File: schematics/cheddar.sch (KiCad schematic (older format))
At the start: 31 parts, among them J1 BATT_CONN, J2 EXTERNAL_TRIGGER, J3 USB_OTG, J4 Conn_01x08, J5 Conn_01x08, Q1 MOSFET_PCH, SW1 SW_Push, U1 ESP-12E, U2 ch340g, U3 MCP73831, U4 HT7333, Y1 12Mhz

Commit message: add symbols to schematic
remove redundant symbol libs (KiCAD version 5 has them already)
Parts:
- removed URLAB-LOGO1: logo, custom-cheddar:urlab, symbol SFE_LOGO_FLAME.1_INCH
- C1, C2, C3, C6, C7, C8, C9: symbol C_Small -> Device:C_Small
- C4, C5: symbol C -> Device:C
- D1: symbol LED_Small -> Device:LED_Small
- D4: symbol D_Schottky -> Device:D_Schottky
- J1, J2: symbol CONN_01X02 -> Connector_Generic:Conn_01x02
- J3: symbol USB_OTG-RESCUE-dash -> Connector:USB_B_Micro
- J4, J5: symbol Conn_01x08 -> Connector_Generic:Conn_01x08
- Q1: symbol MOSFET_PCH-IRLML2244 -> Device:Q_PMOS_GDS
- R2, R3, R5, R6, R7, R8, R9: symbol R_Small -> Device:R_Small
- SW1: symbol SW_Push -> Switch:SW_Push
- U1: symbol ESP-12E -> RF_Module:ESP-12F
- U2: symbol ch340g -> Interface_USB:CH340G
- U3: symbol MCP73831 -> Battery_Management:MCP73831-2-OT
- U4: symbol HT73xx-RESCUE-dash -> Regulator_Linear:AZ1117-3.3
- Y1: symbol Crystal -> Device:Crystal
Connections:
- wire segments 104 -> 131

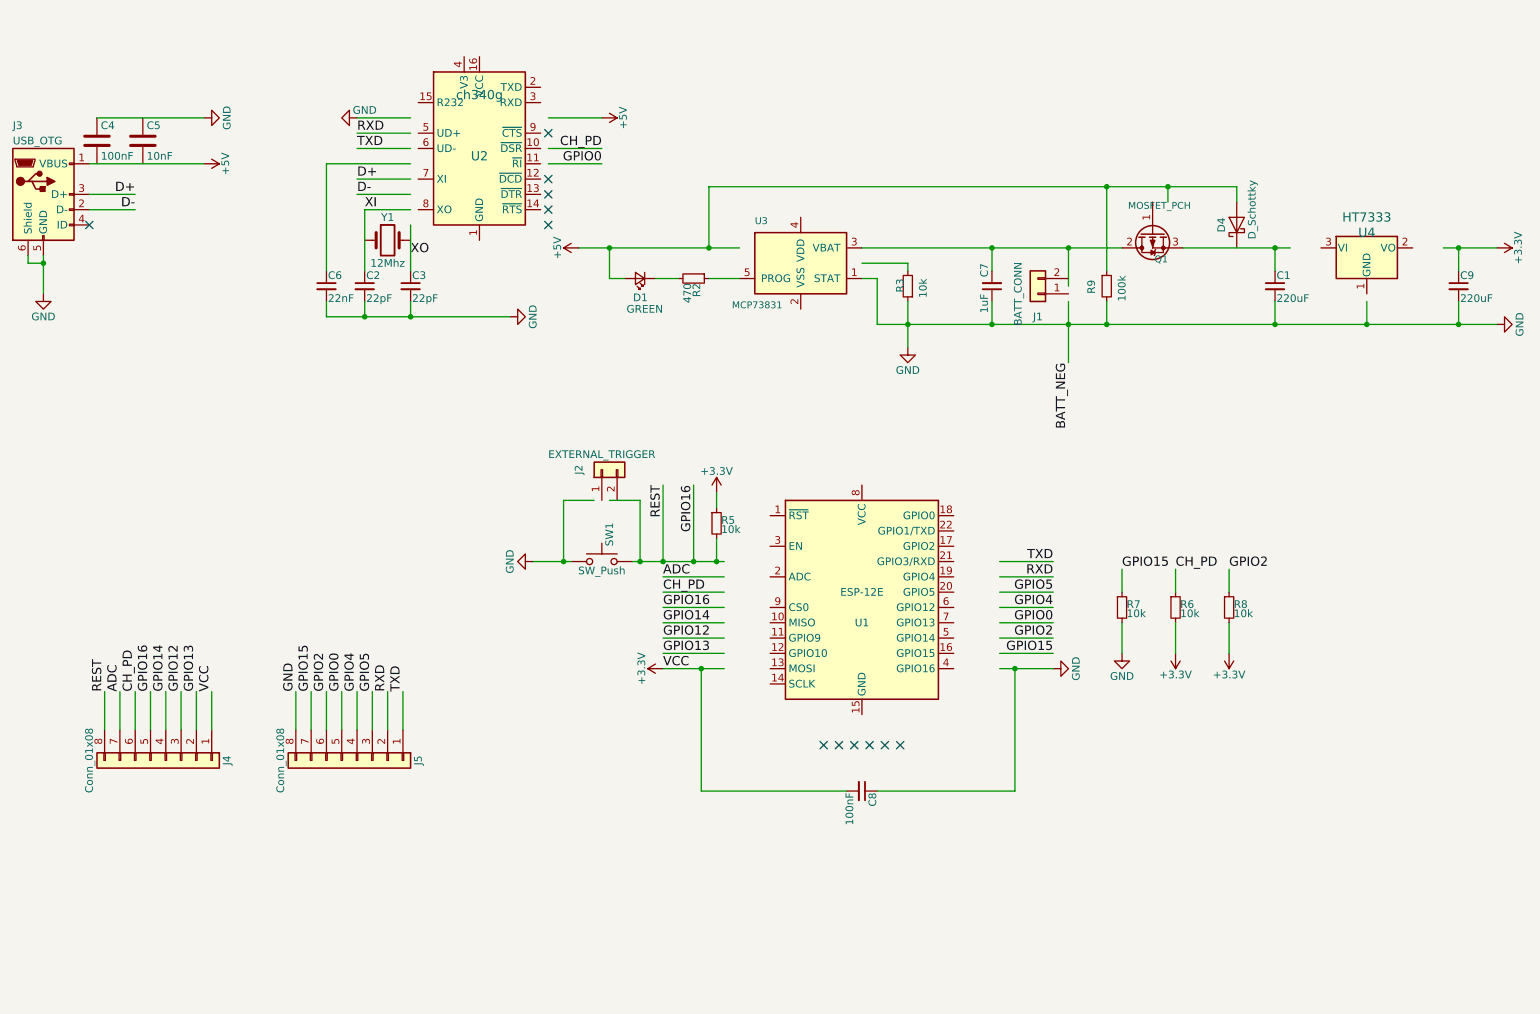
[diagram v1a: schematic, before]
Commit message: fix #8, all components connected
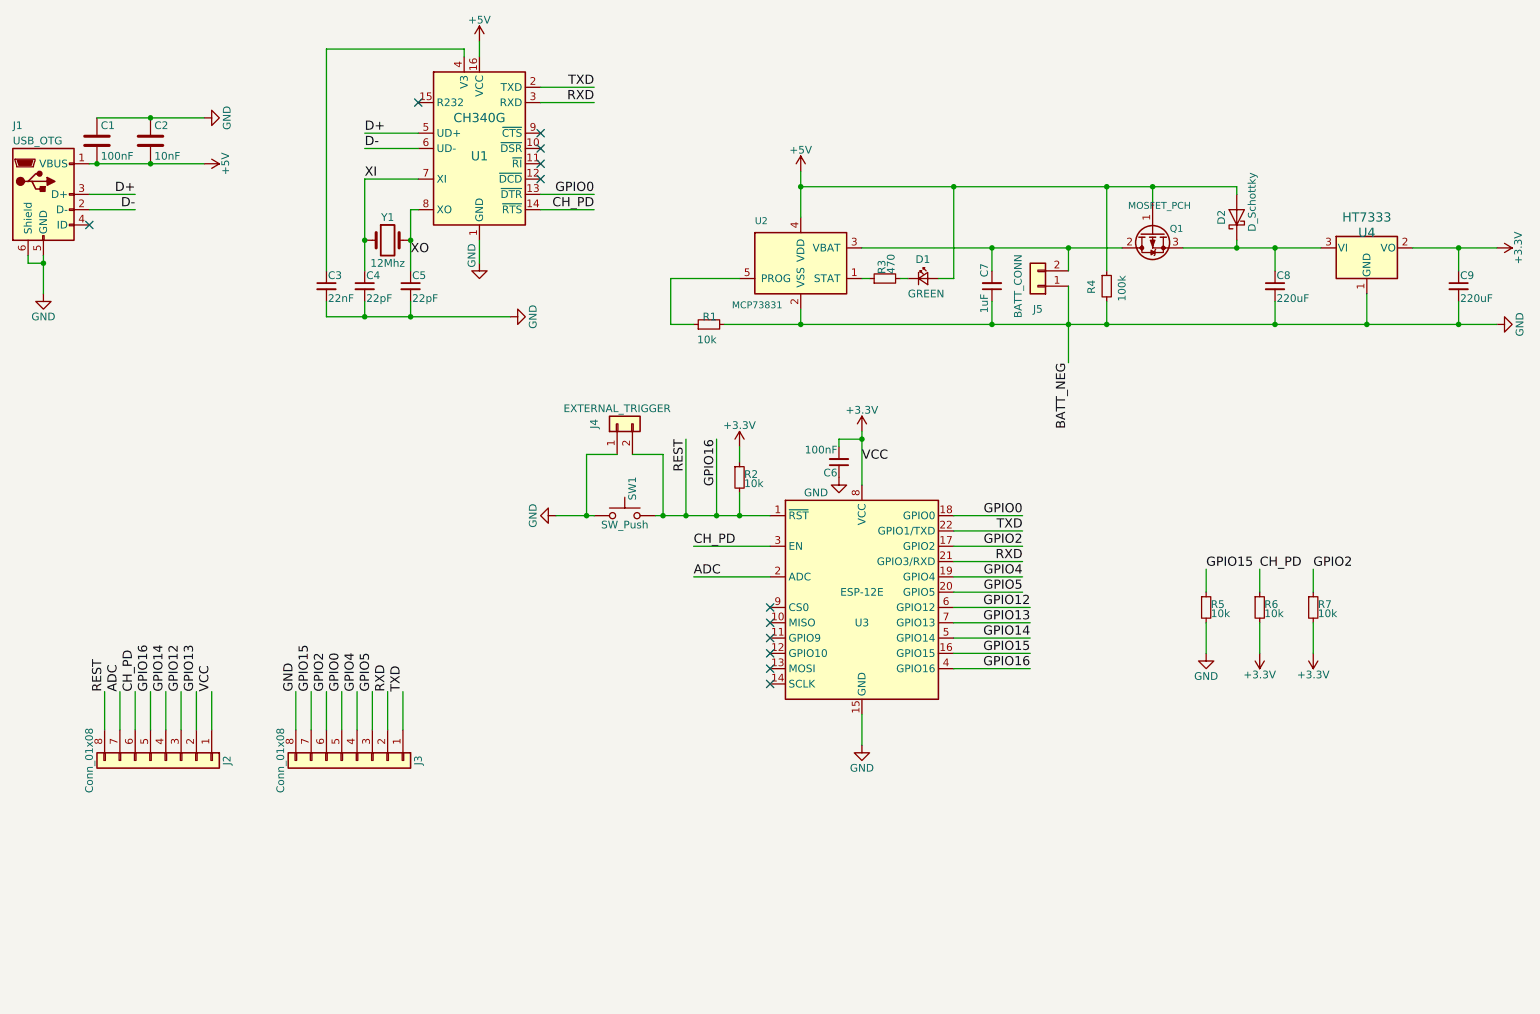
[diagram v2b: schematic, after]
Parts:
- U1: renamed from U2; value ch340g -> CH340G
- renumbered C4 to C1, C5 to C2, C6 to C3, C2 to C4, C3 to C5, C8 to C6, C1 to C8, D4 to D2, J3 to J1, J4 to J2, J5 to J3, J2 to J4, J1 to J5, R3 to R1, R5 to R2, R2 to R3, R9 to R4, R7 to R5, R8 to R7, U3 to U2, U1 to U3
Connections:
- wire segments 131 -> 134
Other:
- moved on the sheet: C2, C6, D1, D2, J4, J5, R1, R2, R3, R5, R6, R7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

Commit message: replace all footprints with standard lib ones
remove unnecessary custom libs
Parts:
- C1, C2, C3, C4, C5, C6, C7, C8, C9: footprint Capacitors_SMD:C_1206_HandSoldering -> Capacitor_SMD:C_1206_3216Metric_Pad1.42x1.75mm_HandSolder
- D1: footprint LEDs:LED_1206 -> LED_SMD:LED_1206_3216Metric
- D2: footprint Diodes_SMD:SOD-523 -> Diode_SMD:D_SOD-523
- J2, J3: footprint Pin_Headers:Pin_Header_Straight_1x08_Pitch2.54mm -> Connector_PinHeader_2.54mm:PinHeader_1x08_P2.54mm_Vertical
- J4: footprint Pin_Headers:Pin_Header_Straight_1x02 -> Connector_PinHeader_2.54mm:PinHeader_1x02_P2.54mm_Vertical
- J5: footprint Connectors_JST:JST_SH_SM02B-SRSS-TB_02x1.00mm_Angled -> Resistor_SMD:R_1206_3216Metric_Pad1.42x1.75mm_HandSolder
- Q1: footprint Silicon-Standard:SOT23-3 -> Package_TO_SOT_SMD:SOT-23_Handsoldering
- R1, R2, R3, R4, R5, R6, R7: footprint Resistors_SMD:R_1206_HandSoldering -> Resistor_SMD:R_1206_3216Metric_Pad1.42x1.75mm_HandSolder
- SW1: footprint Buttons_Switches_SMD:SW_SPST_REED_CT05-XXXX-G1 -> Button_Switch_SMD:SW_SPST_REED_CT05-XXXX-G1
- U1: footprint SMD_Packages:SO-16-N -> Package_SO:SOIC-16_3.9x9.9mm_P1.27mm
- U2: footprint sot:SOT23-5 -> Package_TO_SOT_SMD:SOT-23-5_HandSoldering
- U3: footprint ESP8266:ESP-12E_SMD -> RF_Module:ESP-12E
- U4: footprint sot:SOT89 -> Package_TO_SOT_SMD:SOT-89-3_Handsoldering
- Y1: footprint Clocks:CRYSTAL-SMD-3.2X2.5MM -> custom-cheddar:CRYSTAL-SMD-3.2X2.5MM
